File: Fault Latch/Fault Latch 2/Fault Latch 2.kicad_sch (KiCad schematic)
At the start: 18 parts, among them J1 Inputs, K1 Fujitsu_FTR-LYAA005x, Q2 PMOS, Q3 NMOS, SW2 SW_Push_Dual_x2, U1 LM397, U2 LM397, U3 74LS279, U5 LM397, U6 74LVC1G10, U7 4N35

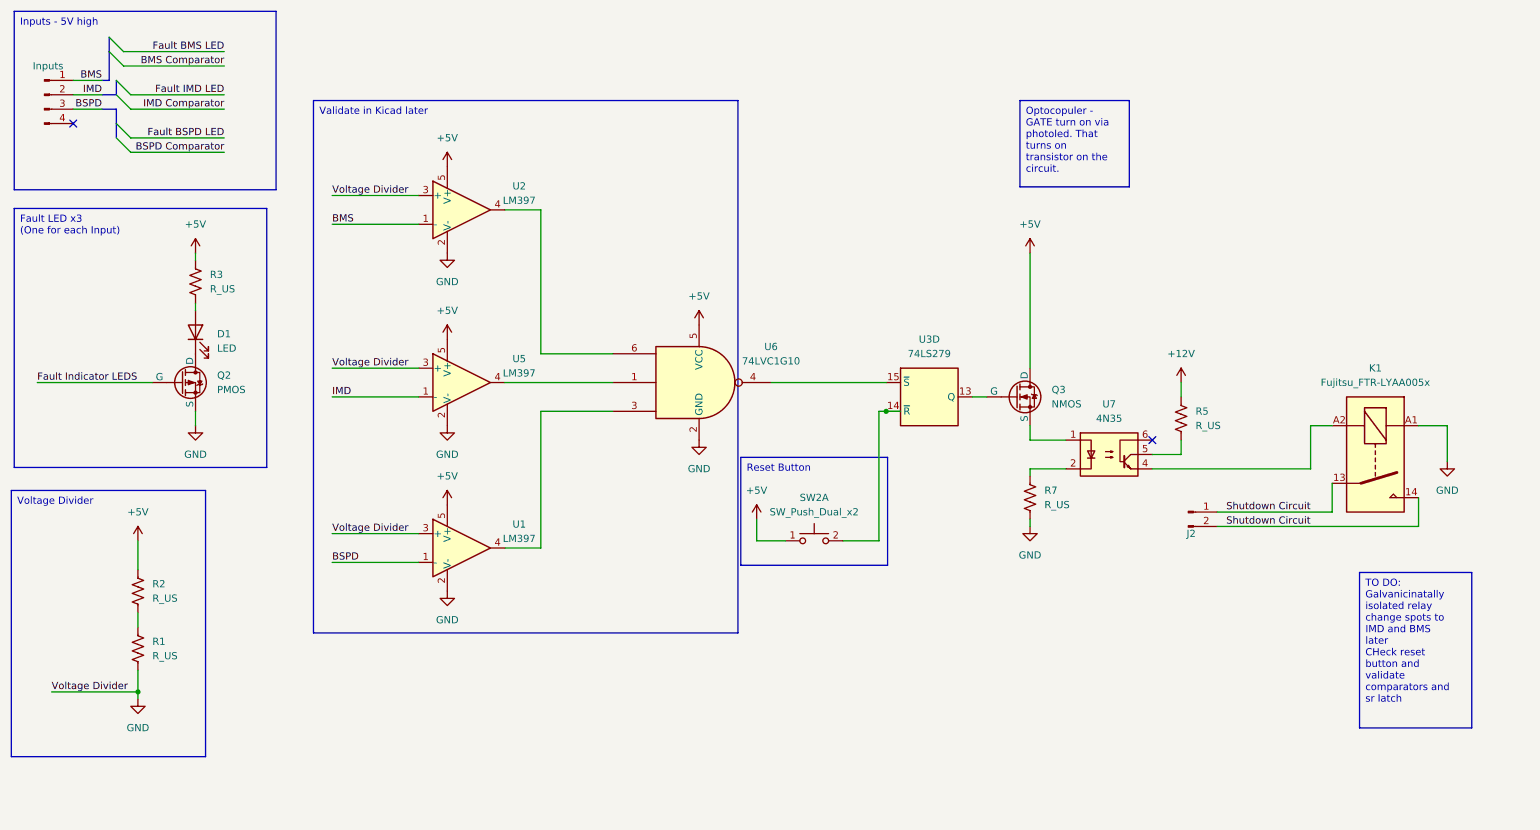
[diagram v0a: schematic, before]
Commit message: To Dos on Fault Latch and RML AGAIN.
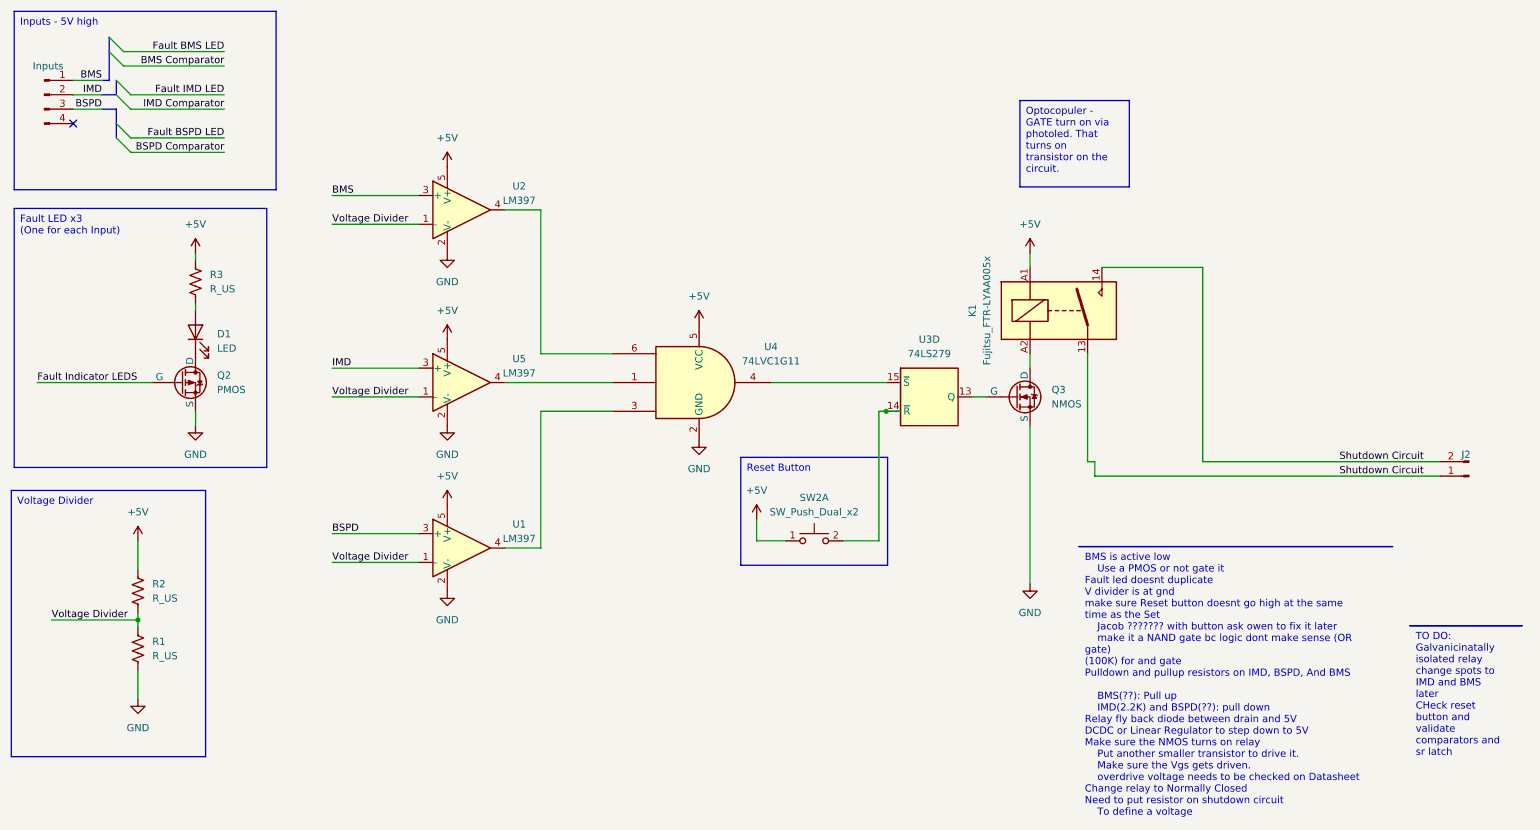
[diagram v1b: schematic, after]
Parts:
- removed R5, R7: R_US, symbol Device:R_US
- removed U6: 74LVC1G10, symbol 74xGxx:74LVC1G10
- removed U7: 4N35, Package_DIP:DIP-6_W7.62mm, symbol Isolator:4N35
- added U4: 74LVC1G11, symbol 74xGxx:74LVC1G11
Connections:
- net +5V: now also K1.A1, U4.5 (VCC); no longer Q3.1 (D)
- net BMS: now also U2.3 (+); no longer U2.1 (-)
- net BSPD: now also U1.3 (+); no longer U1.1 (-)
- net GND: now also Q3.3 (S), U4.2 (GND); no longer K1.A1, U1.3 (+), U2.3 (+), U5.3 (+)
- net IMD: now also U5.3 (+); no longer U5.1 (-)
- net Voltage Divider: now reaches R1.1, R2.2
- net Voltage Divider: now also U1.1 (-), U2.1 (-), U5.1 (-)
- net at K1.A2: now also Q3.1 (D)
- net at U5.4: now also U4.1
- net at U2.4: now also U4.6
- net at U1.4: now also U4.3
- net at U3.15 (~{S}): now also U4.4
- no-connect marks 2 -> 1
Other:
- moved on the sheet: J2, K1

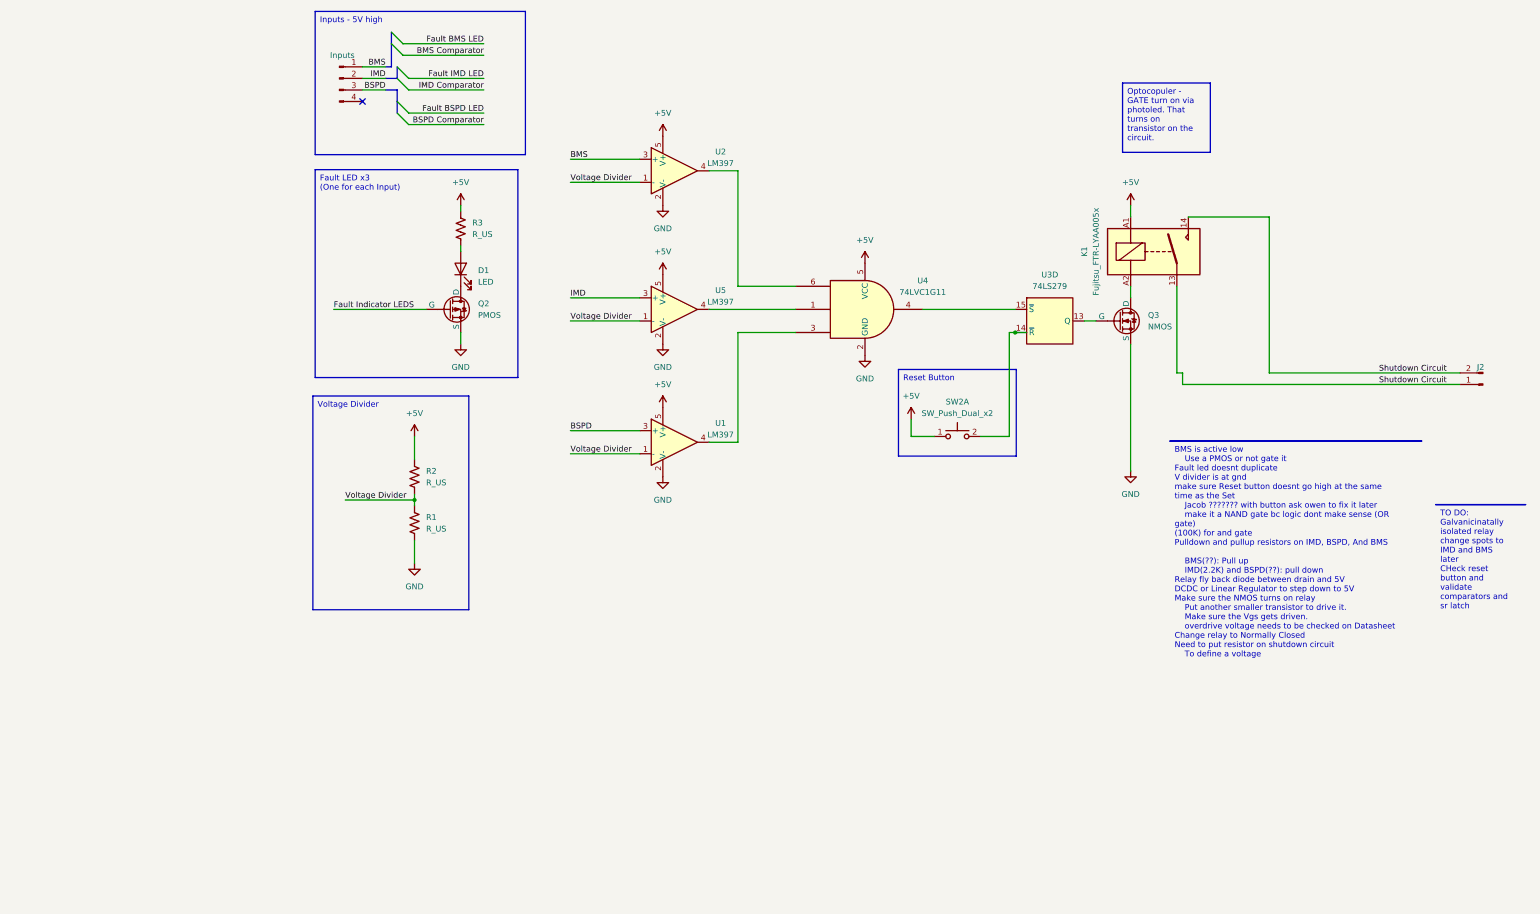
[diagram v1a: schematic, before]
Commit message: Unfinished version of Fault Latch after applying separate circuits
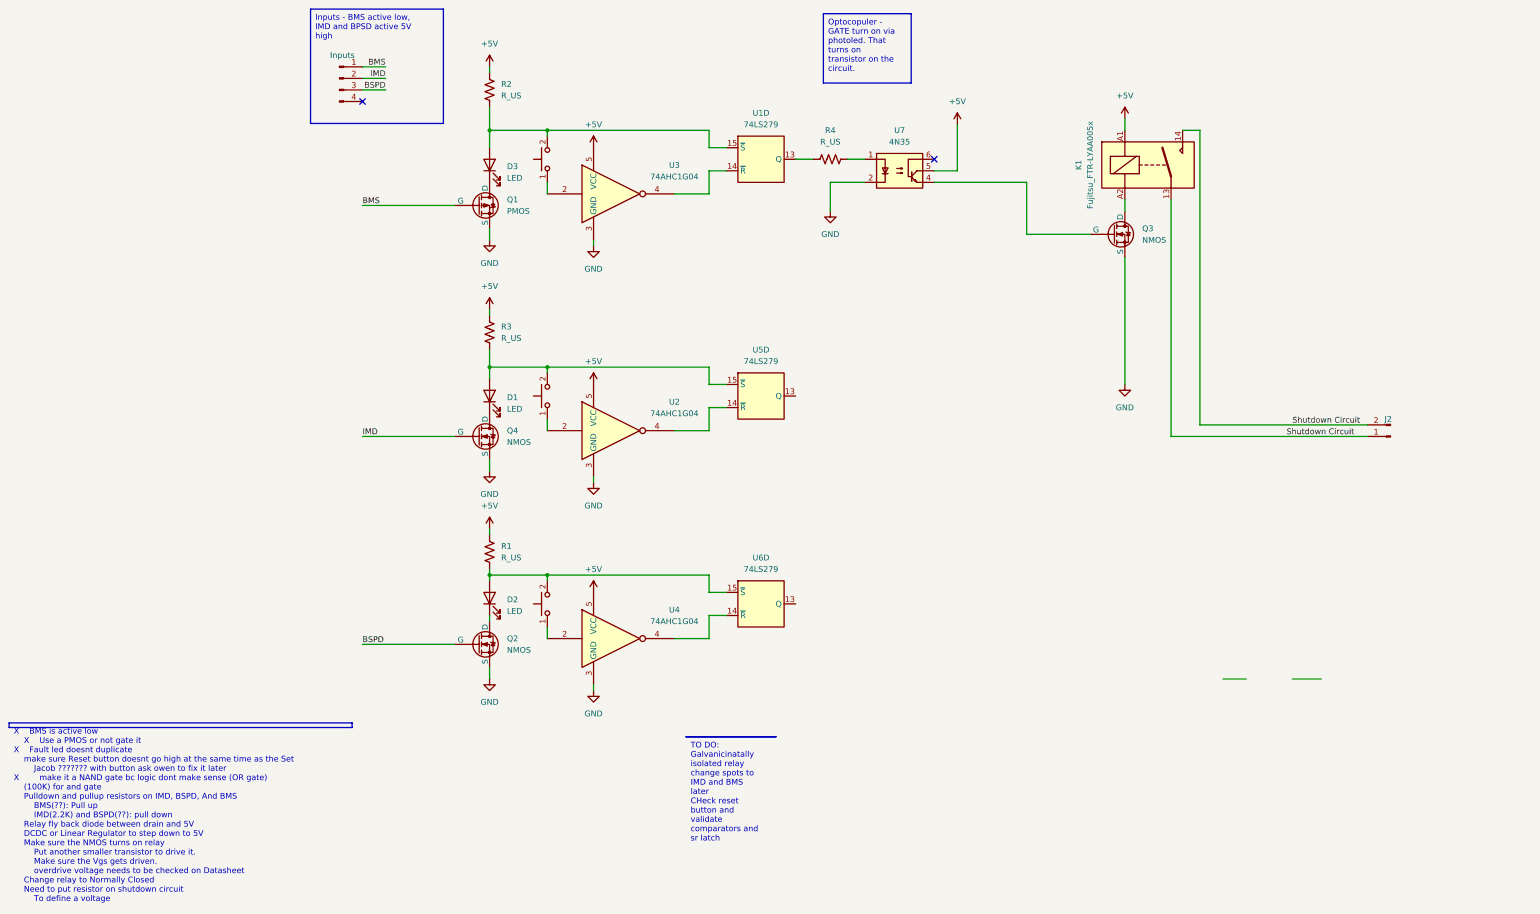
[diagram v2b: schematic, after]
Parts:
- removed Q2: PMOS, symbol Simulation_SPICE:PMOS
- removed U1, U2, U5: LM397, Package_TO_SOT_SMD:SOT-23-5, symbol Comparator:LM397
- removed U3: 74LS279, symbol 74xx:74LS279
- removed U4: 74LVC1G11, symbol 74xGxx:74LVC1G11
- added D2, D3: LED, symbol Device:LED
- added Q1: PMOS, symbol Simulation_SPICE:PMOS
- added Q2, Q4: NMOS, symbol Simulation_SPICE:NMOS
- added R4: R_US, symbol Device:R_US
- added SW1, SW3: SW_Push_Dual_x2, symbol Switch:SW_Push_Dual_x2
- added U1, U5, U6: 74LS279, symbol 74xx:74LS279
- added U2, U3, U4: 74AHC1G04, symbol 74xGxx:74AHC1G04
- added U7: 4N35, Package_DIP:DIP-6_W7.62mm, symbol Isolator:4N35
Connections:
- net +5V: now also R1.1, U2.5 (VCC), U3.5 (VCC), U4.5 (VCC), U7.5; no longer SW2.1 (C)
- net BMS: now also Q1.2 (G)
- net BSPD: now also Q2.2 (G)
- net GND: now also Q1.3 (S), Q2.3 (S), Q4.3 (S), U2.3 (GND), U3.3 (GND), U4.3 (GND), U7.2; no longer R1.2
- net IMD: now also Q4.2 (G)
- net at D1.2 (A), R3.2: now also SW2.2 (D), U5.15 (~{S})
- net at D1.1 (K): now also Q4.1 (D)
- net at Q3.2 (G): now also U7.4
- net Voltage Divider: no longer names the net of R2.2
- net Voltage Divider: now also D3.2 (A), SW1.2 (D), U1.15 (~{S}); no longer R1.1
- new net: U2.4, U5.14 (~{R})
- new net: SW3.1 (C), U4.2
- new net: U4.4, U6.14 (~{R})
- new net: D2.2 (A), R1.2, SW3.2 (D), U6.15 (~{S})
- new net: D3.1 (K), Q1.1 (D)
- new net: D2.1 (K), Q2.1 (D)
- new net: SW1.1 (C), U3.2
- new net: U1.14 (~{R}), U3.4
- new net: SW2.1 (C), U2.2
- new net: R4.2, U7.1
- new net: R4.1, U1.13 (Q)
- no-connect marks 1 -> 2
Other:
- moved on the sheet: D1, J2, K1, Q3, R3

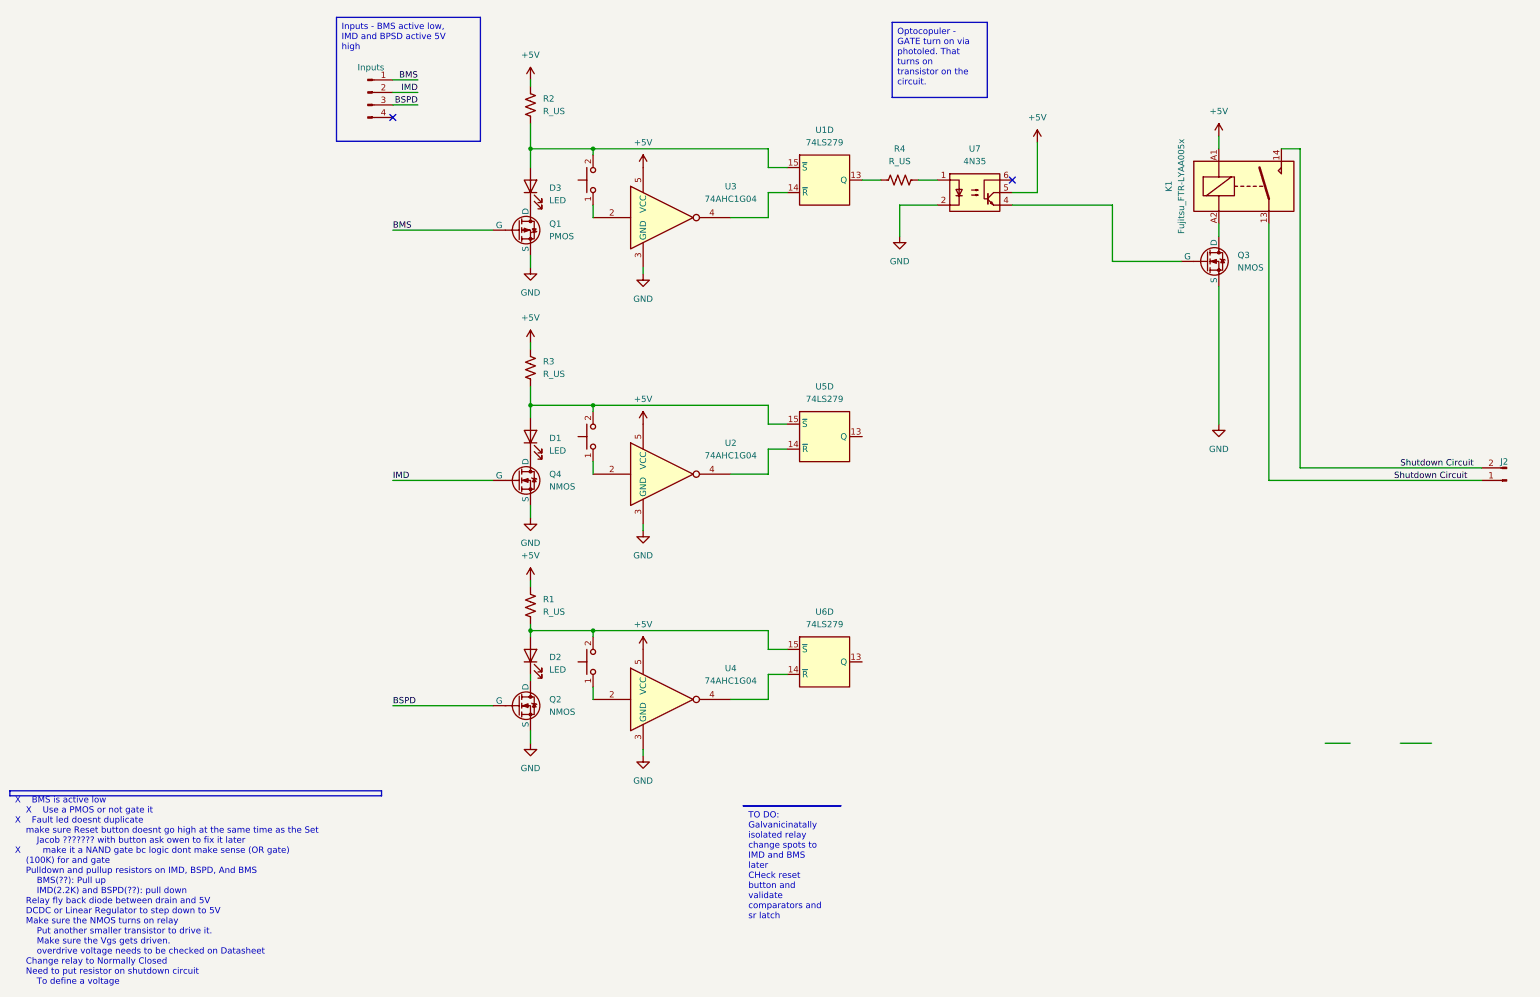
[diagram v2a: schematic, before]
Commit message: Fault Latch Revision without PSpice Check
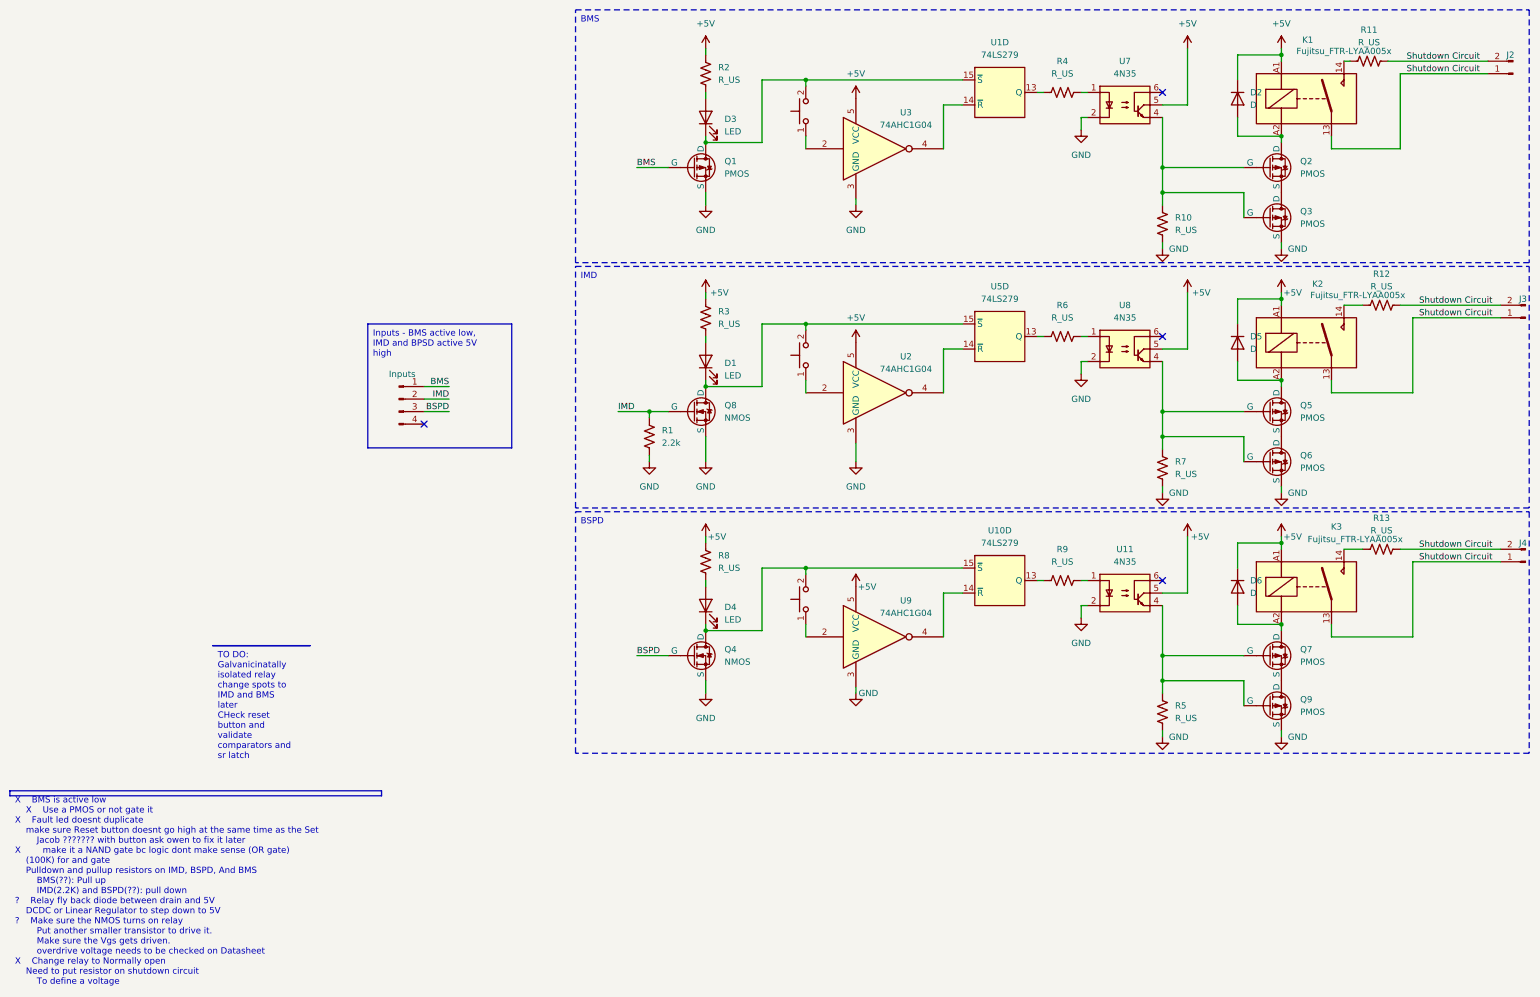
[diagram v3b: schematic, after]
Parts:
- removed D2: LED, symbol Device:LED
- removed Q2, Q3: NMOS, symbol Simulation_SPICE:NMOS
- removed SW3: SW_Push_Dual_x2, symbol Switch:SW_Push_Dual_x2
- removed U4: 74AHC1G04, symbol 74xGxx:74AHC1G04
- removed U6: 74LS279, symbol 74xx:74LS279
- added D2, D5, D6: D, symbol Device:D
- added D4: LED, symbol Device:LED
- added J3, J4: ~, symbol Connector:Conn_01x02_Pin
- added K2, K3: Fujitsu_FTR-LYAA005x, Relay_THT:Relay_SPST-NO_Fujitsu_FTR-LYAA005x_FormA_Vertical, symbol Relay:Fujitsu_FTR-LYAA005x
- added Q2, Q3, Q5, Q6, Q7, Q9: PMOS, symbol Simulation_SPICE:PMOS
- added Q8: NMOS, symbol Simulation_SPICE:NMOS
- added R10, R11, R12, R13, R5, R6, R7, R8, R9: R_US, symbol Device:R_US
- added SW4: SW_Push_Dual_x2, symbol Switch:SW_Push_Dual_x2
- added U10: 74LS279, symbol 74xx:74LS279
- added U11, U8: 4N35, Package_DIP:DIP-6_W7.62mm, symbol Isolator:4N35
- added U9: 74AHC1G04, symbol 74xGxx:74AHC1G04
- R1: value R_US -> 2.2k
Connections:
- net +5V: now also D2.1 (K), D5.1 (K), D6.1 (K), K2.A1, K3.A1, R8.1, U11.5, U8.5, U9.5 (VCC); no longer R1.1
- net BSPD: now also Q4.2 (G)
- net GND: now also R1.2, Q3.3 (S), Q6.3 (S), Q8.3 (S), Q9.3 (S), R10.1, R5.1, R7.1, U11.2, U8.2, U9.3 (GND)
- net IMD: now also R1.1, Q8.2 (G); no longer Q4.2 (G)
- net Shutdown Circuit: now also J3.1 (Pin_1), J3.2 (Pin_2), J4.1 (Pin_1), J4.2 (Pin_2), K2.13, K3.13, R11.2, R12.2, R13.2; no longer K1.14
- net at U5.13 (Q): now also R6.1
- net at SW2.2 (D), U5.15 (~{S}): now also D1.1 (K), Q8.1 (D); no longer D1.2 (A), R3.2
- net at K1.A2: now also D2.2 (A), Q2.1 (D)
- net at Q4.1 (D): now also D4.1 (K), SW4.2 (D), U10.15 (~{S}); no longer D1.1 (K)
- net at D3.1 (K), Q1.1 (D): now also SW1.2 (D), U1.15 (~{S})
- net at D3.2 (A), R2.2: no longer SW1.2 (D), U1.15 (~{S})
- net at U7.4: now also Q2.2 (G), Q3.2 (G), R10.2
- new net: D4.2 (A), R8.2
- new net: K1.14, R11.1
- new net: Q2.3 (S), Q3.1 (D)
- new net: R6.2, U8.1
- new net: Q5.2 (G), Q6.2 (G), R7.2, U8.4
- new net: D1.2 (A), R3.2
- new net: SW4.1 (C), U9.2
- new net: U10.14 (~{R}), U9.4
- new net: Q7.2 (G), Q9.2 (G), R5.2, U11.4
- new net: D6.2 (A), K3.A2, Q7.1 (D)
- new net: Q7.3 (S), Q9.1 (D)
- new net: R9.1, U10.13 (Q)
- new net: R9.2, U11.1
- new net: K2.14, R12.1
- new net: K3.14, R13.1
- new net: Q5.3 (S), Q6.1 (D)
- new net: D5.2 (A), K2.A2, Q5.1 (D)
- no-connect marks 2 -> 4
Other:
- moved on the sheet: D3, J2, K1, Q1, R2, R4, U1D, U3, U7
